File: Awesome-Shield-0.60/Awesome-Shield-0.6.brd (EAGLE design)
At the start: 51 x 55 mm, 21 parts, among them J1 PORT1, SW1 SPST_TACT-EVQQ2, SW2 DPDT, U1 LIGHTSENSORTEMT6000

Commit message: routing 90%, but to be stashed as components move again
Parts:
- moved C1 1.90 mm to (28.6, 41.3), turned to 0 degrees
- moved J2 1.27 mm to (7.62, 22.9)
- moved J3 1.27 mm to (7.62, 40.6)
- moved FID4 1.27 mm to (2.54, 48.3)
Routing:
- net +5V: track 3.54 -> 92.0 mm
- net A0: track 50.4 -> 36.8 mm
- net SCL: track 77.8 -> 90.4 mm
- net D6: track 36.4 -> 34.7 mm
- net A2: track 68.7 -> 67.4 mm
- net D4: track 61.3 -> 60.4 mm
- net IOREF: track 39.8 -> 40.7 mm, vias 0 -> 1

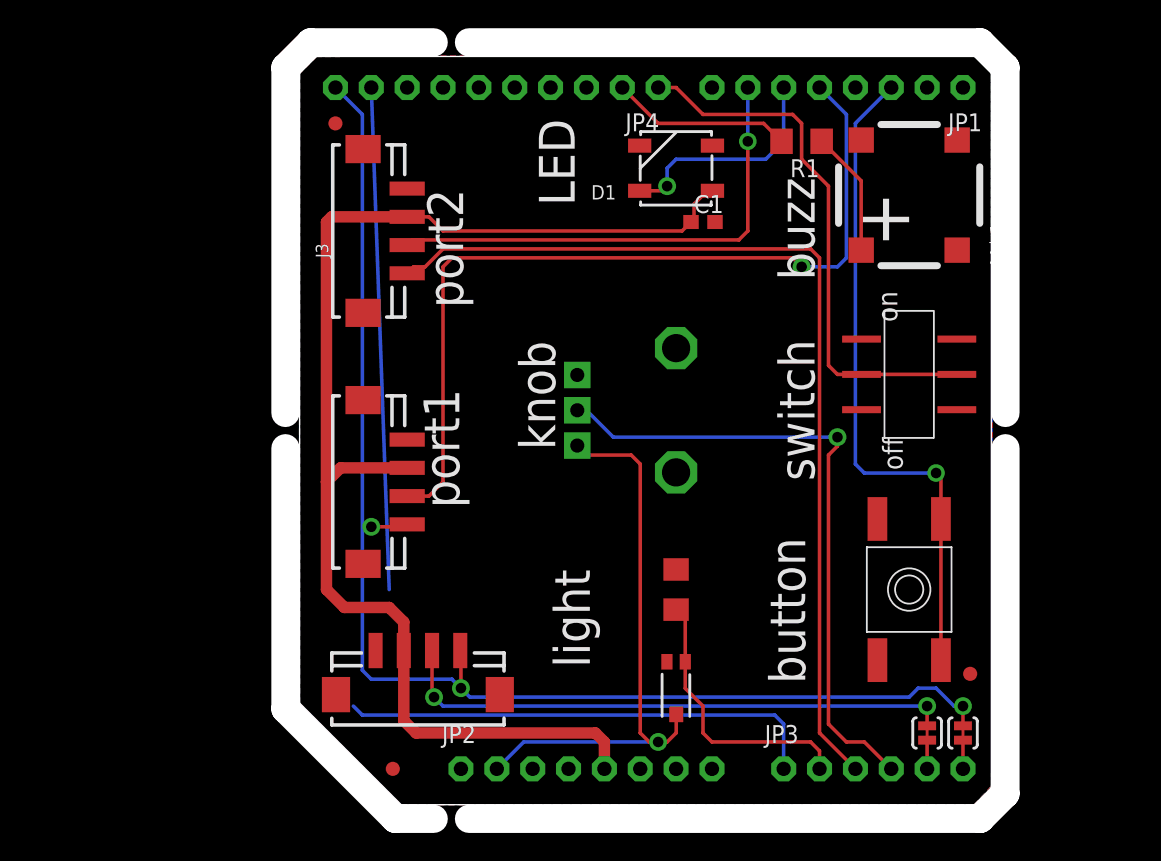
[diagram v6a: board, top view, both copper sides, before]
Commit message: no airwires left, GND established :shipit:
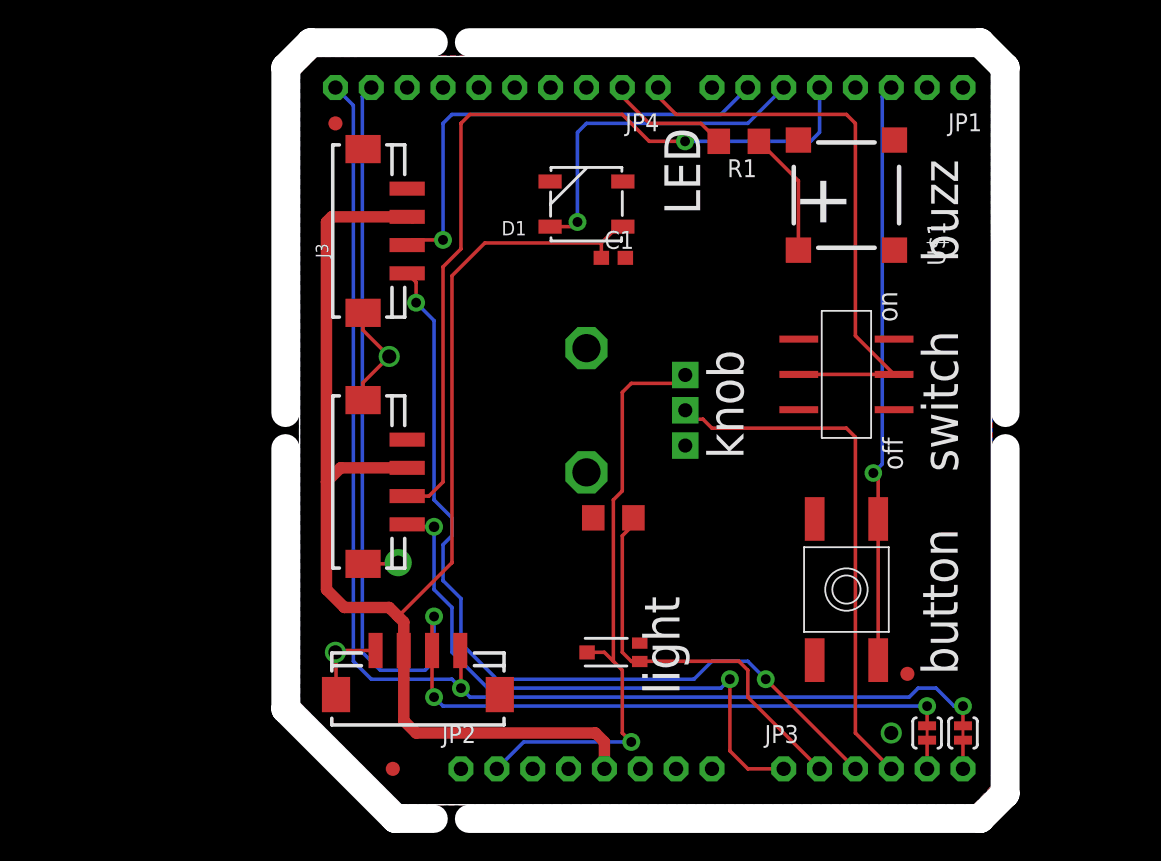
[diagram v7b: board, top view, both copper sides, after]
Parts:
- moved D1 6.84 mm to (20.3, 42.5)
- moved C1 6.84 mm to (22.2, 38.7)
- moved R6 6.75 mm to (22.2, 20.3), turned to 180 degrees
- moved RV1 6.35 mm to (20.3, 27.9), turned to 0 degrees
- moved U1 5.12 mm to (22.2, 10.8), turned to 180 degrees
- moved R1 4.45 mm to (31.1, 47.0)
- moved FID3 4.45 mm to (43.1, 9.27)
- moved SW1 4.45 mm to (38.7, 15.2)
- moved SW2 4.45 mm to (38.7, 30.5)
- moved U$1 4.45 mm to (38.7, 43.2)
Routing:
- net +5V: track 92.0 -> 109.3 mm
- net SDA: track 75.5 -> 91.7 mm, vias 2 -> 3
- net GND: track 0.00 -> 16.1 mm, vias 0 -> 4
- net A1: track 19.6 -> 28.4 mm
- net A3: track 45.6 -> 37.4 mm, vias 1 -> 0
- net D5: track 16.2 -> 24.3 mm
- net A2: track 67.4 -> 61.0 mm, vias 0 -> 2
- net D2: track 47.1 -> 41.2 mm
- net A0: track 36.8 -> 42.2 mm, vias 1 -> 2
- net D9: track 12.9 -> 8.78 mm
- net D8: track 38.5 -> 41.1 mm
- net IOREF: track 40.7 -> 43.0 mm
- net D4: track 60.4 -> 58.8 mm
- net D6: track 34.7 -> 33.6 mm
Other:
- board text removed: "port1"
- board text removed: "port2"

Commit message: added large round silkscreen around LED, solved #31
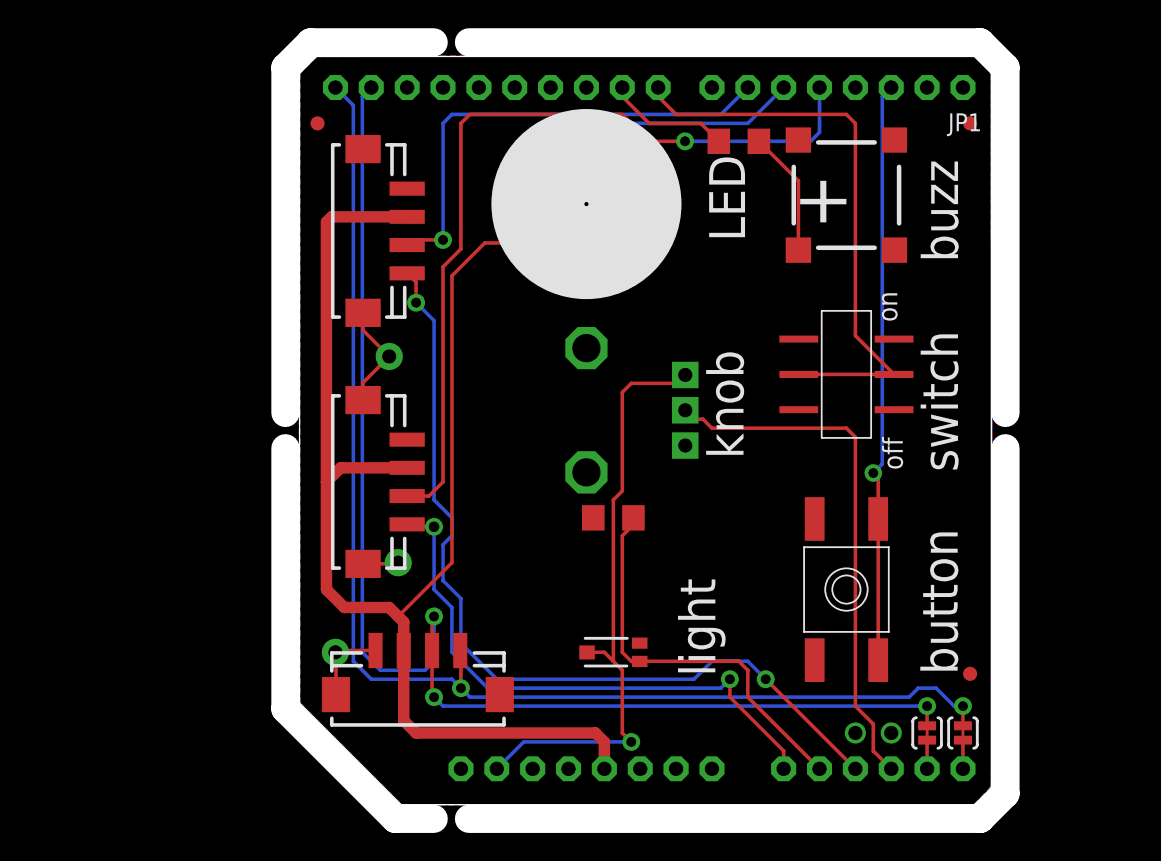
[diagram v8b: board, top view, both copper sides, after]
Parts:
- J2: value (none) -> PORT2
- J3: value (none) -> PORT3
- moved FID1 61.3 mm to (47.5, 48.3)
- moved FID3 4.44 mm to (47.5, 9.27)
- moved FID4 1.27 mm to (1.27, 48.3)
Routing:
- net A0: track 42.2 -> 40.7 mm
- net GND: vias 4 -> 5
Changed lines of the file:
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@@
 <setting verticaltext="up"/>
 </settings>
-<grid distance="0.025" unitdist="inch" unit="inch" style="lines" multiple="1" display="yes" altdistance="0.01" altunitdist="inch" altunit="inch"/>
+<grid distance="1" unitdist="mm" unit="mm" style="lines" multiple="1" display="yes" altdistance="0.1" altunitdist="mm" altunit="mm"/>
 <layers>
 <layer number="1" name="Top" color="4" fill="1" visible="yes" active="yes"/>
@@
 <layer number="19" name="Unrouted" color="6" fill="1" visible="yes" active="yes"/>
 <layer number="20" name="Dimension" color="15" fill="1" visible="yes" active="yes"/>
-<layer number="21" name="tPlace" color="16" fill="1" visible="yes" active="yes"/>
-<layer number="22" name="bPlace" color="14" fill="1" visible="yes" active="yes"/>
+<layer number="21" name="tPlace" color="16" fill="1" visible="no" active="yes"/>
+<layer number="22" name="bPlace" color="14" fill="1" visible="no" active="yes"/>
 <layer number="23" name="tOrigins" color="15" fill="1" visible="yes" active="yes"/>
 <layer number="24" name="bOrigins" color="15" fill="1" visible="yes" active="yes"/>
@@
 <text x="46.615" y="9.211" size="2.54" layer="25" font="vector" rot="R90">button</text>
 <text x="28.905" y="32.213" size="2.54" layer="25" font="vector" rot="R270">knob</text>
-<text x="24.372" y="14.761" size="2.54" layer="25" font="vector" rot="R270">light</text>
+<text x="26.912" y="16.031" size="2.54" layer="25" font="vector" rot="R270">light</text>
 <text x="46.64210625" y="38.42526875" size="2.54" layer="25" font="vector" rot="SR90">buzz</text>
-<text x="25.838" y="47.939" size="2.54" layer="25" font="vector" rot="R270">LED</text>
+<text x="29.013" y="46.034" size="2.54" layer="25" font="vector" rot="R270">LED</text>
 <text x="42.34" y="34.19" size="1.4224" layer="25" font="vector" rot="SR90">on</text>
 <text x="42.728" y="23.706" size="1.4224" layer="25" font="vector" rot="SR90">off</text>
@@
 <wire x1="-1" y1="52.22" x2="-1" y2="27.75" width="2" layer="46"/>
 <wire x1="-1" y1="25.25" x2="-1" y2="6.78" width="2" layer="46"/>
+<circle x="20.32" y="42.545" radius="5.462475" width="2.54" layer="21"/>
+<circle x="20.32" y="42.545" radius="3.419578125" width="2.54" layer="21"/>
+<circle x="20.32" y="42.545" radius="1.419903125" width="2.54" layer="21"/>
 </plain>
 <attributes>
@@
 <attribute name="VALUE" x="10.287" y="8.509" size="0.889" layer="27" font="vector" ratio="11" rot="R180"/>
 </element>
-<element name="J2" library="Seeed-OPL-Connector" package="HW4-SMD-2.0" value="" x="7.62" y="22.86" smashed="yes" rot="R90">
+<element name="J2" library="Seeed-OPL-Connector" package="HW4-SMD-2.0" value="PORT2" x="7.62" y="22.86" smashed="yes" rot="R90">
 <attribute name="VALUE" x="5.207" y="20.955" size="0.889" layer="27" font="vector" ratio="11" rot="R90"/>
 </element>
-<element name="FID1" library="SparkFun-Aesthetics" package="FIDUCIAL-1X2" value="FIDUCIAL1X2" x="6.604" y="2.54"/>
-<element name="FID3" library="SparkFun-Aesthetics" package="FIDUCIAL-1X2" value="FIDUCIAL1X2" x="43.055" y="9.27"/>
-<element name="FID4" library="SparkFun-Aesthetics" package="FIDUCIAL-1X2" value="FIDUCIAL1X2" x="2.54" y="48.26"/>
+<element name="FID1" library="SparkFun-Aesthetics" package="FIDUCIAL-1X2" value="FIDUCIAL1X2" x="47.498" y="48.26"/>
+<element name="FID3" library="SparkFun-Aesthetics" package="FIDUCIAL-1X2" value="FIDUCIAL1X2" x="47.498" y="9.271"/>
+<element name="FID4" library="SparkFun-Aesthetics" package="FIDUCIAL-1X2" value="FIDUCIAL1X2" x="1.27" y="48.26"/>
 <element name="U1" library="SparkFun-Sensors" package="TEMT6000-SEN" value="LIGHTSENSORTEMT6000" x="22.225" y="10.795" smashed="yes" rot="R180"/>
-<element name="JP4" library="adafruit" package="1X10-BIG" value="PINHD-1X10" x="13.97" y="50.8" rot="R180"/>
+<element name="JP4" library="adafruit" package="1X10-BIG" value="PINHD-1X10" x="13.97" y="50.8" smashed="yes" rot="R180"/>
 <element name="JP1" library="adafruit" package="1X08-CLEANBIG" value="" x="38.1" y="50.8" rot="R180"/>
-<element name="JP2" library="adafruit" package="1X08-CLEANBIG" value="" x="20.32" y="2.54"/>
-<element name="JP3" library="adafruit" package="1X06-CLEAN" value="" x="40.64" y="2.54"/>
-<element name="J3" library="Seeed-OPL-Connector" package="HW4-SMD-2.0" value="" x="7.62" y="40.64" rot="R90"/>
-<element name="D1" library="SparkFun-LED" package="WS2812B" value="" x="20.32" y="42.545" rot="R180">
+<element name="JP2" library="adafruit" package="1X08-CLEANBIG" value="" x="20.32" y="2.54" smashed="yes">
+<attribute name="VALUE" x="10.16" y="-0.635" size="1.27" layer="27"/>
+</element>
+<element name="JP3" library="adafruit" package="1X06-CLEAN" value="" x="40.64" y="2.54" smashed="yes">
+<attribute name="VALUE" x="33.02" y="-0.635" size="1.27" layer="27"/>
+</element>
+<element name="J3" library="Seeed-OPL-Connector" package="HW4-SMD-2.0" value="PORT3" x="7.62" y="40.64" smashed="yes" rot="R90">
+<attribute name="VALUE" x="5.207" y="38.735" size="0.889" layer="27" font="vector" ratio="11" rot="R90"/>
+</element>
+<element name="D1" library="SparkFun-LED" package="WS2812B" value="" x="20.32" y="42.545" smashed="yes" rot="R180">
 <attribute name="PROD_ID" value="DIO-12503" x="20.32" y="42.545" size="1.778" layer="27" font="vector" ratio="15" rot="R180" display="off"/>
+<attribute name="VALUE" x="16.066" y="44.145" size="0.6096" layer="27" rot="R180"/>
 </element>
-<element name="C1" library="rcl" package="C0603" value="100nF" x="22.225" y="38.735"/>
-<element name="R1" library="rcl" package="R1206" value="TBD" x="31.115" y="46.99" rot="R180"/>
-<element name="U$1" library="buzzer-loudity-bzel-t68-0808" package="SMT-68" value="LOUDITY-BZEL-T680808" x="38.735" y="43.18" rot="R90"/>
+<element name="C1" library="rcl" package="C0603" value="100nF" x="22.225" y="38.735" smashed="yes"/>
+<element name="R1" library="rcl" package="R1206" value="TBD" x="31.115" y="46.99" smashed="yes" rot="R180"/>
+<element name="U$1" library="buzzer-loudity-bzel-t68-0808" package="SMT-68" value="LOUDITY-BZEL-T680808" x="38.735" y="43.18" smashed="yes" rot="R90"/>
 </elements>
 <signals>
@@
 <wire x1="2.582" y1="7.799" x2="2.582" y2="10.753" width="0.254" layer="1"/>
 <wire x1="2.582" y1="10.753" x2="2.54" y2="10.795" width="0.254" layer="1"/>
-<via x="2.54" y="10.795" extent="1-16" drill="1" diameter="1"/>
+<via x="2.54" y="10.795" extent="1-16" drill="1" diameter="1.9304"/>
 <wire x1="5.382" y1="10.922" x2="2.667" y2="10.922" width="0.254" layer="1"/>
 <wire x1="2.667" y1="10.922" x2="2.54" y2="10.795" width="0.254" layer="1"/>
 <wire x1="4.497" y1="34.84" x2="4.497" y2="33.603" width="0.254" layer="1"/>
 <wire x1="4.497" y1="33.603" x2="6.35" y2="31.75" width="0.254" layer="1"/>
-<via x="6.35" y="31.75" extent="1-16" drill="1" diameter="1"/>
+<via x="6.35" y="31.75" extent="1-16" drill="1" diameter="1.9304"/>
 <wire x1="6.35" y1="31.75" x2="4.497" y2="29.897" width="0.254" layer="1"/>
 <wire x1="4.497" y1="29.897" x2="4.497" y2="28.66" width="0.254" layer="1"/>
 <via x="41.91" y="5.08" extent="1-16" drill="1" diameter="1"/>
+<via x="39.37" y="5.08" extent="1-16" drill="1" diameter="1"/>
 </signal>
 <signal name="D2">
@@
 <wire x1="9.525" y1="19.685" x2="7.445" y2="19.685" width="0.254" layer="1"/>
 <wire x1="7.445" y1="19.685" x2="7.62" y2="19.86" width="0.254" layer="1"/>
-<wire x1="34.29" y1="2.54" x2="31.75" y2="2.54" width="0.254" layer="1"/>
-<wire x1="31.75" y1="2.54" x2="30.48" y2="3.81" width="0.254" layer="1"/>
-<wire x1="30.48" y1="3.81" x2="30.48" y2="8.89" width="0.254" layer="1"/>
 <via x="30.48" y="8.89" extent="1-16" drill="0.7" diameter="1.27"/>
 <wire x1="30.48" y1="8.89" x2="29.845" y2="8.255" width="0.254" layer="16"/>
@@
 <wire x1="10.795" y1="13.97" x2="9.525" y2="15.24" width="0.254" layer="16"/>
 <wire x1="9.525" y1="15.24" x2="9.525" y2="19.685" width="0.254" layer="16"/>
+<wire x1="34.29" y1="2.54" x2="34.29" y2="3.81" width="0.254" layer="1"/>
+<wire x1="34.29" y1="3.81" x2="30.48" y2="7.62" width="0.254" layer="1"/>
+<wire x1="30.48" y1="7.62" x2="30.48" y2="8.89" width="0.254" layer="1"/>
 </signal>
 <signal name="A5">
@@
 <contactref element="RV1" pad="P$2"/>
 <contactref element="JP3" pad="4"/>
-<wire x1="41.91" y1="2.54" x2="39.37" y2="5.08" width="0.254" layer="1"/>
-<wire x1="39.37" y1="5.08" x2="39.37" y2="26.035" width="0.254" layer="1"/>
+<wire x1="39.37" y1="6.985" x2="39.37" y2="26.035" width="0.254" layer="1"/>
 <wire x1="39.37" y1="26.035" x2="38.735" y2="26.67" width="0.254" layer="1"/>
 <wire x1="38.735" y1="26.67" x2="29.21" y2="26.67" width="0.254" layer="1"/>
@@
 <wire x1="28.575" y1="27.305" x2="27.955" y2="27.305" width="0.254" layer="1"/>
 <wire x1="27.955" y1="27.305" x2="27.32" y2="27.94" width="0.254" layer="1"/>
+<wire x1="39.37" y1="6.985" x2="40.64" y2="5.715" width="0.254" layer="1"/>
+<wire x1="40.64" y1="5.715" x2="40.64" y2="3.81" width="0.254" layer="1"/>
+<wire x1="40.64" y1="3.81" x2="41.91" y2="2.54" width="0.254" layer="1"/>
 </signal>
 <signal name="IOREF">
